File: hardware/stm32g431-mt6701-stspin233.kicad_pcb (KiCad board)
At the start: 4 copper layers, 40.1 x 39.8 mm, 90 parts, among them J101 I2C, J102 UART, J103 CANBUS_IN, J104 CANBUS_OUT, J106 CAN TERMINATION, J107 EXT_PWR, J109 MOT_FPC, J110 MOT_FPC2, J201 STDC14, J601 USB_C_Receptacle_USB2.0, Q501 AO3400A, SW201 DFU, SW202 RESET, U101 SN65HVD230, U201 STM32G431, U301 STSPIN233, U401 MT6701, U501 GC9A01, U601 SRV05-4, U701 XC6206, Y201 12MHz

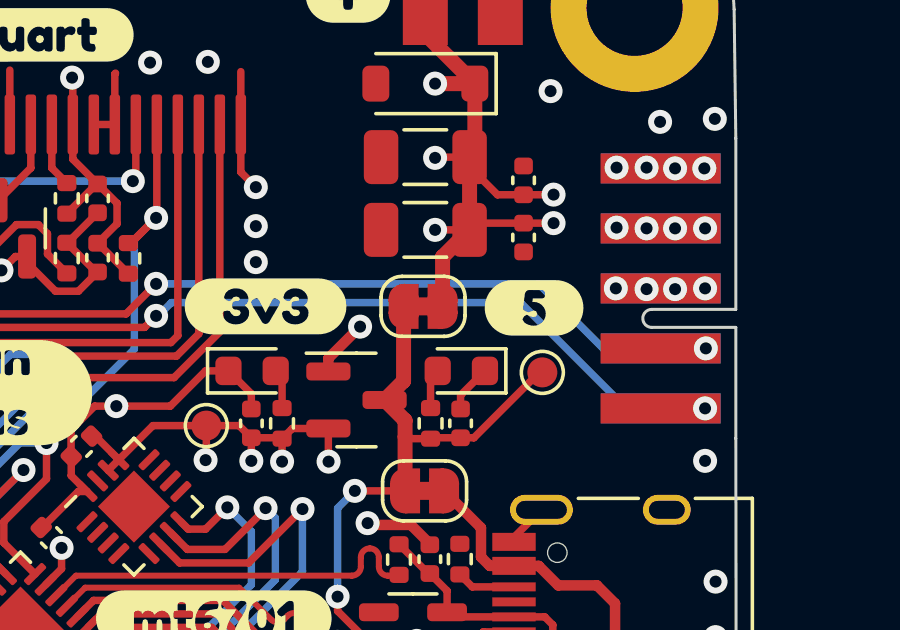
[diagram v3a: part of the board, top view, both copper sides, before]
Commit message: prototype canbus unique id search
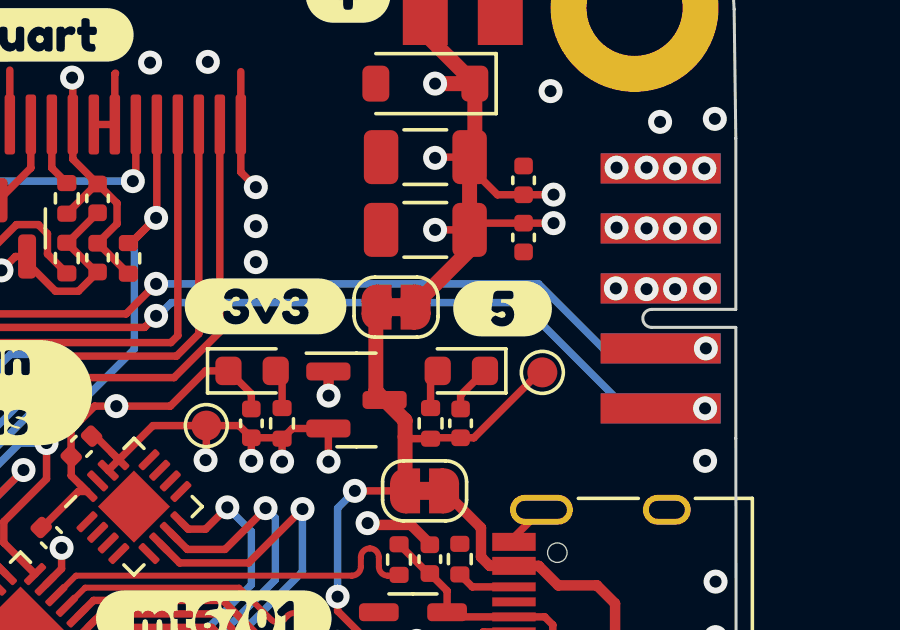
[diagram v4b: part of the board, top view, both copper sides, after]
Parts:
- moved kibuzzard-649D0025 1.05 mm to (140.6, 60.7)
- moved JP701 0.90 mm to (137.0, 60.6)
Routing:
- net GND: track 76.1 -> 75.0 mm
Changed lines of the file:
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@@
   )
   (footprint "kibuzzard-649D0025" (layer "F.Cu")
-    (at 141.6 60.65)
+    (at 140.55 60.675)
     (descr "Generated with KiBuzzard")
     (tags "kb_params=eyJBbGlnbm1lbnRDaG9pY2UiOiAiQ2VudGVyIiwgIkNhcExlZnRDaG9pY2UiOiAiKCIsICJDYXBSaWdodENob2ljZSI6ICIpIiwgIkZvbnRDb21ib0JveCI6ICJGcmVkb2thT25lIiwgIkhlaWdodEN0cmwiOiAiMSIsICJMYXllckNvbWJvQm94IjogIkYuU2lsa1MiLCAiTXVsdGlMaW5lVGV4dCI6ICI1IiwgIlBhZGRpbmdCb3R0b21DdHJsIjogIjUiLCAiUGFkZGluZ0xlZnRDdHJsIjogIjUiLCAiUGFkZGluZ1JpZ2h0Q3RybCI6ICI1IiwgIlBhZGRpbmdUb3BDdHJsIjogIjUiLCAiV2lkdGhDdHJsIjogIiJ9")
@@
   )
   (footprint "Jumper:SolderJumper-2_P1.3mm_Bridged_RoundedPad1.0x1.5mm" (layer "F.Cu")
-    (at 137.9 60.6 180)
+    (at 137 60.625 180)
     (descr "SMD Solder Jumper, 1x1.5mm, rounded Pads, 0.3mm gap, bridged with 1 copper strip")
     (tags "net tie solder jumper bridged")
@@
   (segment (start 130.65 62.75) (end 129.475 63.925) (width 0.25) (layer "F.Cu") (net 2))
   (segment (start 118.926421 78.687183) (end 118.926421 80.044827) (width 0.25) (layer "F.Cu") (net 2))
+  (segment (start 134.75 63.575) (end 134.75 62.7775) (width 0.35) (layer "F.Cu") (net 2))
   (segment (start 116.375 79.675) (end 116.95 79.675) (width 0.25) (layer "F.Cu") (net 2))
   (segment (start 117.835589 72.65208) (end 117.835589 72.710589) (width 0.25) (layer "F.Cu") (net 2))
@@
   (segment (start 137.175 81.85) (end 138 81.85) (width 0.35) (layer "F.Cu") (net 2))
   (segment (start 118.910624 80.060624) (end 118.846248 80.125) (width 0.25) (layer "F.Cu") (net 2))
+  (segment (start 134.75 62.7775) (end 134.7425 62.77) (width 0.35) (layer "F.Cu") (net 2))
   (segment (start 126.025 58.48) (end 126.05 58.48) (width 0.25) (layer "F.Cu") (net 2))
   (segment (start 124.7 58.9375) (end 124.30885 58.9375) (width 0.25) (layer "F.Cu") (net 2))
@@
   (segment (start 127.625 52.85) (end 127.65 52.825) (width 0.25) (layer "F.Cu") (net 2))
   (segment (start 125.939193 80.294416) (end 126.137888 80.493111) (width 0.25) (layer "F.Cu") (net 2))
-  (segment (start 134.7425 62.77) (end 134.7425 62.333) (width 0.35) (layer "F.Cu") (net 2))
   (segment (start 139.07 74.93) (end 139.125 74.985) (width 0.25) (layer "F.Cu") (net 2))
   (segment (start 127 59.455) (end 127.05 59.455) (width 0.25) (layer "F.Cu") (net 2))
@@
   (segment (start 126.171178 66.244338) (end 126.171178 65.603822) (width 0.25) (layer "F.Cu") (net 2))
   (segment (start 133.9275 79.6) (end 133.925 79.6) (width 0.25) (layer "F.Cu") (net 2))
-  (segment (start 134.7425 62.333) (end 135.8 61.2755) (width 0.35) (layer "F.Cu") (net 2))
   (segment (start 128.971258 77.303742) (end 129.6 76.675) (width 0.25) (layer "F.Cu") (net 2))
   (segment (start 135.305 75.925) (end 135.809071 75.925) (width 0.25) (layer "F.Cu") (net 2))
@@
   (via (at 128.8 52.475) (size 0.8) (drill 0.4) (layers "F.Cu" "B.Cu") (free) (net 2))
   (via (at 128.7 85.875) (size 0.8) (drill 0.4) (layers "F.Cu" "B.Cu") (free) (net 2))
-  (via (at 135.8 61.2755) (size 0.8) (drill 0.4) (layers "F.Cu" "B.Cu") (net 2))
+  (via (at 134.75 63.575) (size 0.8) (drill 0.4) (layers "F.Cu" "B.Cu") (net 2))
   (via (at 147.625 54.35) (size 0.8) (drill 0.4) (layers "F.Cu" "B.Cu") (free) (net 2))
   (via (at 109.675 74.125) (size 0.8) (drill 0.4) (layers "F.Cu" "B.Cu") (free) (net 2))
@@
   (segment (start 137.81 77.7) (end 138.16 78.05) (width 0.25) (layer "F.Cu") (net 8))
   (segment (start 136.89 77.7875) (end 136.9775 77.7) (width 0.25) (layer "F.Cu") (net 8))
-  (segment (start 138.55 60.6) (end 138.55 58.95) (width 0.5) (layer "F.Cu") (net 9))
   (segment (start 139.45 55.95) (end 139.45 55.625) (width 0.25) (layer "F.Cu") (net 9))
   (segment (start 139.45 58.05) (end 138.3 58.05) (width 0.25) (layer "F.Cu") (net 9))
@@
   (segment (start 137.975 50.9) (end 137.974693 50.900307) (width 0.5) (layer "F.Cu") (net 9))
   (segment (start 140.38 56.88) (end 139.45 55.95) (width 0.25) (layer "F.Cu") (net 9))
+  (segment (start 137.65 60.625) (end 137.65 60.525) (width 0.5) (layer "F.Cu") (net 9))
   (segment (start 137.974693 50.899693) (end 137.975 50.9) (width 0.5) (layer "F.Cu") (net 9))
   (segment (start 132.22 84.105) (end 133.375 82.95) (width 0.35) (layer "F.Cu") (net 9))
@@
   (segment (start 133.165 82.74) (end 133.375 82.95) (width 0.25) (layer "F.Cu") (net 9))
   (segment (start 133.165 81.075) (end 133.165 82.74) (width 0.25) (layer "F.Cu") (net 9))
+  (segment (start 139.45 58.725) (end 139.45 58.05) (width 0.5) (layer "F.Cu") (net 9))
   (segment (start 139.625 53.175) (end 138.3 53.175) (width 0.5) (layer "F.Cu") (net 9))
   (segment (start 141.25 56.88) (end 140.38 56.88) (width 0.25) (layer "F.Cu") (net 9))
   (segment (start 131.95 84.105) (end 132.22 84.105) (width 0.35) (layer "F.Cu") (net 9))
   (segment (start 139.45 55.625) (end 139.45 58.05) (width 0.5) (layer "F.Cu") (net 9))
+  (segment (start 137.65 60.525) (end 139.45 58.725) (width 0.5) (layer "F.Cu") (net 9))
   (segment (start 137.974693 51.524693) (end 139.625 53.175) (width 0.5) (layer "F.Cu") (net 9))
   (segment (start 137.974693 50.900307) (end 137.974693 51.524693) (width 0.5) (layer "F.Cu") (net 9))
-  (segment (start 138.55 58.95) (end 139.45 58.05) (width 0.5) (layer "F.Cu") (net 9))
   (segment (start 141.25 57.825) (end 142.25 57.825) (width 0.25) (layer "F.Cu") (net 9))
   (segment (start 141.25 57.825) (end 139.675 57.825) (width 0.25) (layer "F.Cu") (net 9))
@@
   (segment (start 139.595 64.98) (end 141.775 62.8) (width 0.25) (layer "F.Cu") (net 12))
   (segment (start 141.775 62.8) (end 141.875 62.8) (width 0.25) (layer "F.Cu") (net 12))
+  (segment (start 136.325 63.4275) (end 136.6175 63.72) (width 0.5) (layer "F.Cu") (net 12))
   (segment (start 139.15 64.98) (end 139.595 64.98) (width 0.25) (layer "F.Cu") (net 12))
   (segment (start 137.3 64.95) (end 137.3 64.4025) (width 0.5) (layer "F.Cu") (net 12))
@@
   (segment (start 137.3 66.75) (end 137.3 64.95) (width 0.5) (layer "F.Cu") (net 12))
   (segment (start 137.36 65.01) (end 137.3 64.95) (width 0.25) (layer "F.Cu") (net 12))
+  (segment (start 136.325 60.65) (end 136.325 63.4275) (width 0.5) (layer "F.Cu") (net 12))
   (segment (start 138.15 65.01) (end 137.36 65.01) (width 0.25) (layer "F.Cu") (net 12))
   (segment (start 138.18 64.98) (end 138.15 65.01) (width 0.25) (layer "F.Cu") (net 12))
   (segment (start 135.050535 70.754786) (end 136.040749 71.745) (width 0.25) (layer "F.Cu") (net 12))
-  (segment (start 137.25 60.6) (end 137.25 63.0875) (width 0.5) (layer "F.Cu") (net 12))
+  (segment (start 136.35 60.625) (end 136.325 60.65) (width 0.5) (layer "F.Cu") (net 12))
   (segment (start 135.050535 70.275381) (end 135.050535 70.754786) (width 0.25) (layer "F.Cu") (net 12))
   (segment (start 137.3 64.4025) (end 136.6175 63.72) (width 0.5) (layer "F.Cu") (net 12))
-  (segment (start 137.25 63.0875) (end 136.6175 63.72) (width 0.5) (layer "F.Cu") (net 12))
   (segment (start 135.625 66.75) (end 137.3 66.75) (width 0.25) (layer "F.Cu") (net 12))
   (segment (start 136.040749 71.745) (end 136.425 71.745) (width 0.25) (layer "F.Cu") (net 12))
